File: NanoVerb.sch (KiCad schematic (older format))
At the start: 2 parts, among them U6 7805

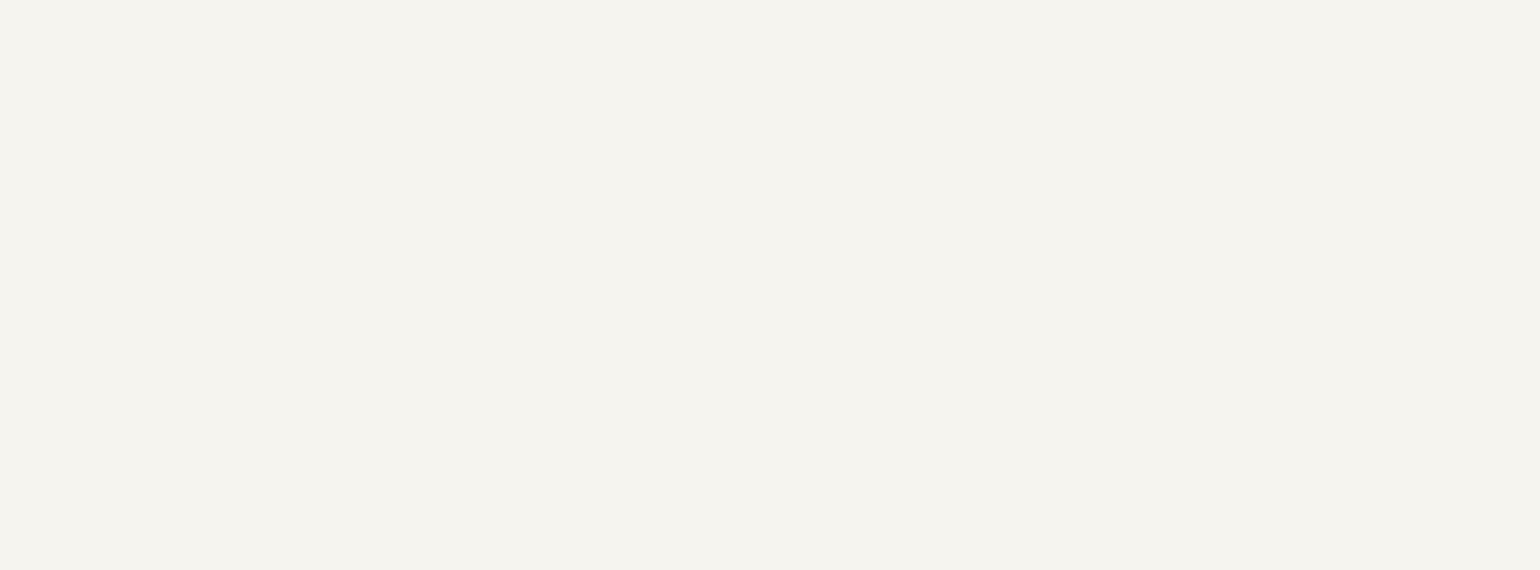
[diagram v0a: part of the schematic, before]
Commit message: Adding a few component symbols to the schematics (U9 and U8 OpAmps)
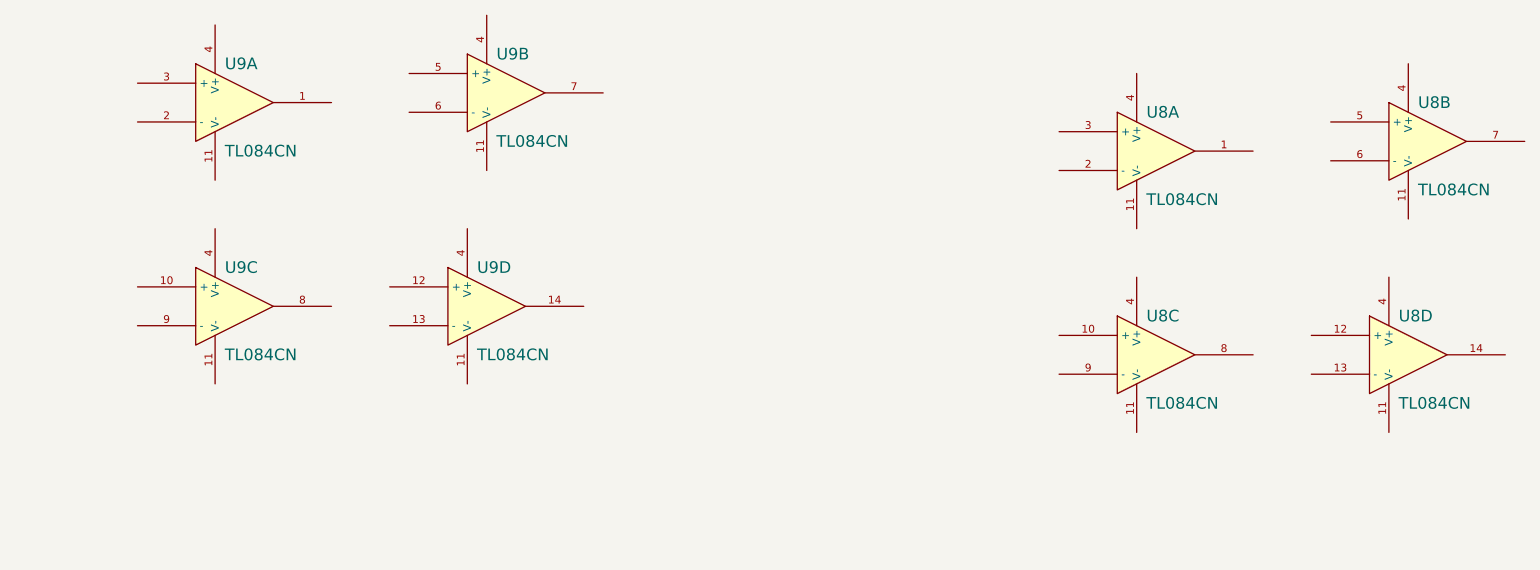
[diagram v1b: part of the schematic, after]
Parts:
- added U8, U9: TL084CN, symbol TL084CN
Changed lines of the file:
@@
 LIBS:valves
 LIBS:s87c51
+LIBS:tl084cn
 LIBS:NanoVerb-cache
 EELAYER 25 0
@@
 	1    0    0    -1
 $EndComp
+$Comp
+L TL084CN U9
+U 1 1 54A6F65E
+P 9150 2400
+F 0 "U9" H 9100 2600 60  0000 L CNN
+F 1 "TL084CN" H 9100 2150 60  0000 L CNN
+F 2 "" H 9150 2400 60  0000 C CNN
+F 3 "" H 9150 2400 60  0000 C CNN
+	1    9150 2400
+	1    0    0    -1
+$EndComp
+$Comp
+L TL084CN U9
+U 3 1 54A6F6C1
+P 9150 3450
+F 0 "U9" H 9100 3650 60  0000 L CNN
+F 1 "TL084CN" H 9100 3200 60  0000 L CNN
+F 2 "" H 9150 3450 60  0000 C CNN
+F 3 "" H 9150 3450 60  0000 C CNN
+	3    9150 3450
+	1    0    0    -1
+$EndComp
+$Comp
+L TL084CN U9
+U 4 1 54A6F6FF
+P 10450 3450
+F 0 "U9" H 10400 3650 60  0000 L CNN
+F 1 "TL084CN" H 10400 3200 60  0000 L CNN
+F 2 "" H 10450 3450 60  0000 C CNN
+F 3 "" H 10450 3450 60  0000 C CNN
+	4    10450 3450
+	1    0    0    -1
+$EndComp
+$Comp
+L TL084CN U9
+U 2 1 54A6F73C
+P 10550 2350
+F 0 "U9" H 10500 2550 60  0000 L CNN
+F 1 "TL084CN" H 10500 2100 60  0000 L CNN
+F 2 "" H 10550 2350 60  0000 C CNN
+F 3 "" H 10550 2350 60  0000 C CNN
+	2    10550 2350
+	1    0    0    -1
+$EndComp
+$Comp
+L TL084CN U8
+U 1 1 54A6FB5C
+P 13900 2650
+F 0 "U8" H 13850 2850 60  0000 L CNN
+F 1 "TL084CN" H 13850 2400 60  0000 L CNN
+F 2 "" H 13900 2650 60  0000 C CNN
+F 3 "" H 13900 2650 60  0000 C CNN
+	1    13900 2650
+	1    0    0    -1
+$EndComp
+$Comp
+L TL084CN U8
+U 3 1 54A6FB62
+P 13900 3700
+F 0 "U8" H 13850 3900 60  0000 L CNN
+F 1 "TL084CN" H 13850 3450 60  0000 L CNN
+F 2 "" H 13900 3700 60  0000 C CNN
+F 3 "" H 13900 3700 60  0000 C CNN
+	3    13900 3700
+	1    0    0    -1
+$EndComp
+$Comp
+L TL084CN U8
+U 4 1 54A6FB68
+P 15200 3700
+F 0 "U8" H 15150 3900 60  0000 L CNN
+F 1 "TL084CN" H 15150 3450 60  0000 L CNN
+F 2 "" H 15200 3700 60  0000 C CNN
+F 3 "" H 15200 3700 60  0000 C CNN
+	4    15200 3700
+	1    0    0    -1
+$EndComp
+$Comp
+L TL084CN U8
+U 2 1 54A6FB6E
+P 15300 2600
+F 0 "U8" H 15250 2800 60  0000 L CNN
+F 1 "TL084CN" H 15250 2350 60  0000 L CNN
+F 2 "" H 15300 2600 60  0000 C CNN
+F 3 "" H 15300 2600 60  0000 C CNN
+	2    15300 2600
+	1    0    0    -1
+$EndComp

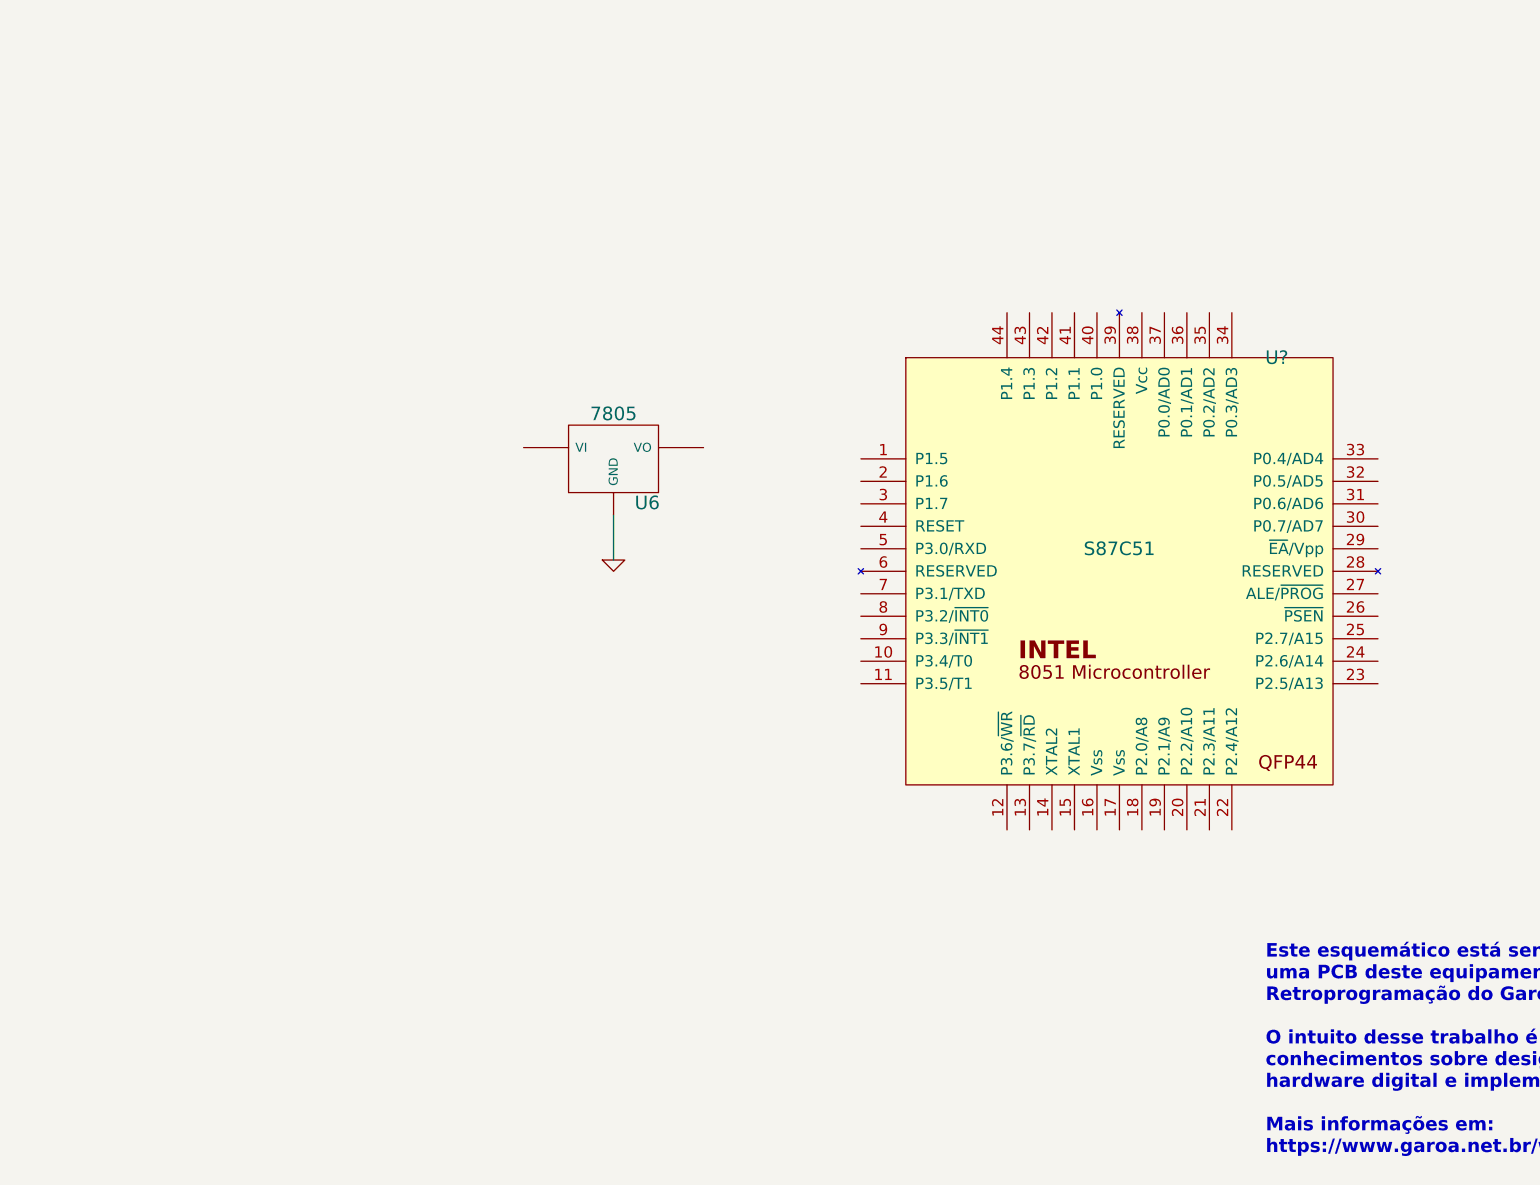
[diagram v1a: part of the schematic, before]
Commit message: updating schematics drawing with DRAM IC
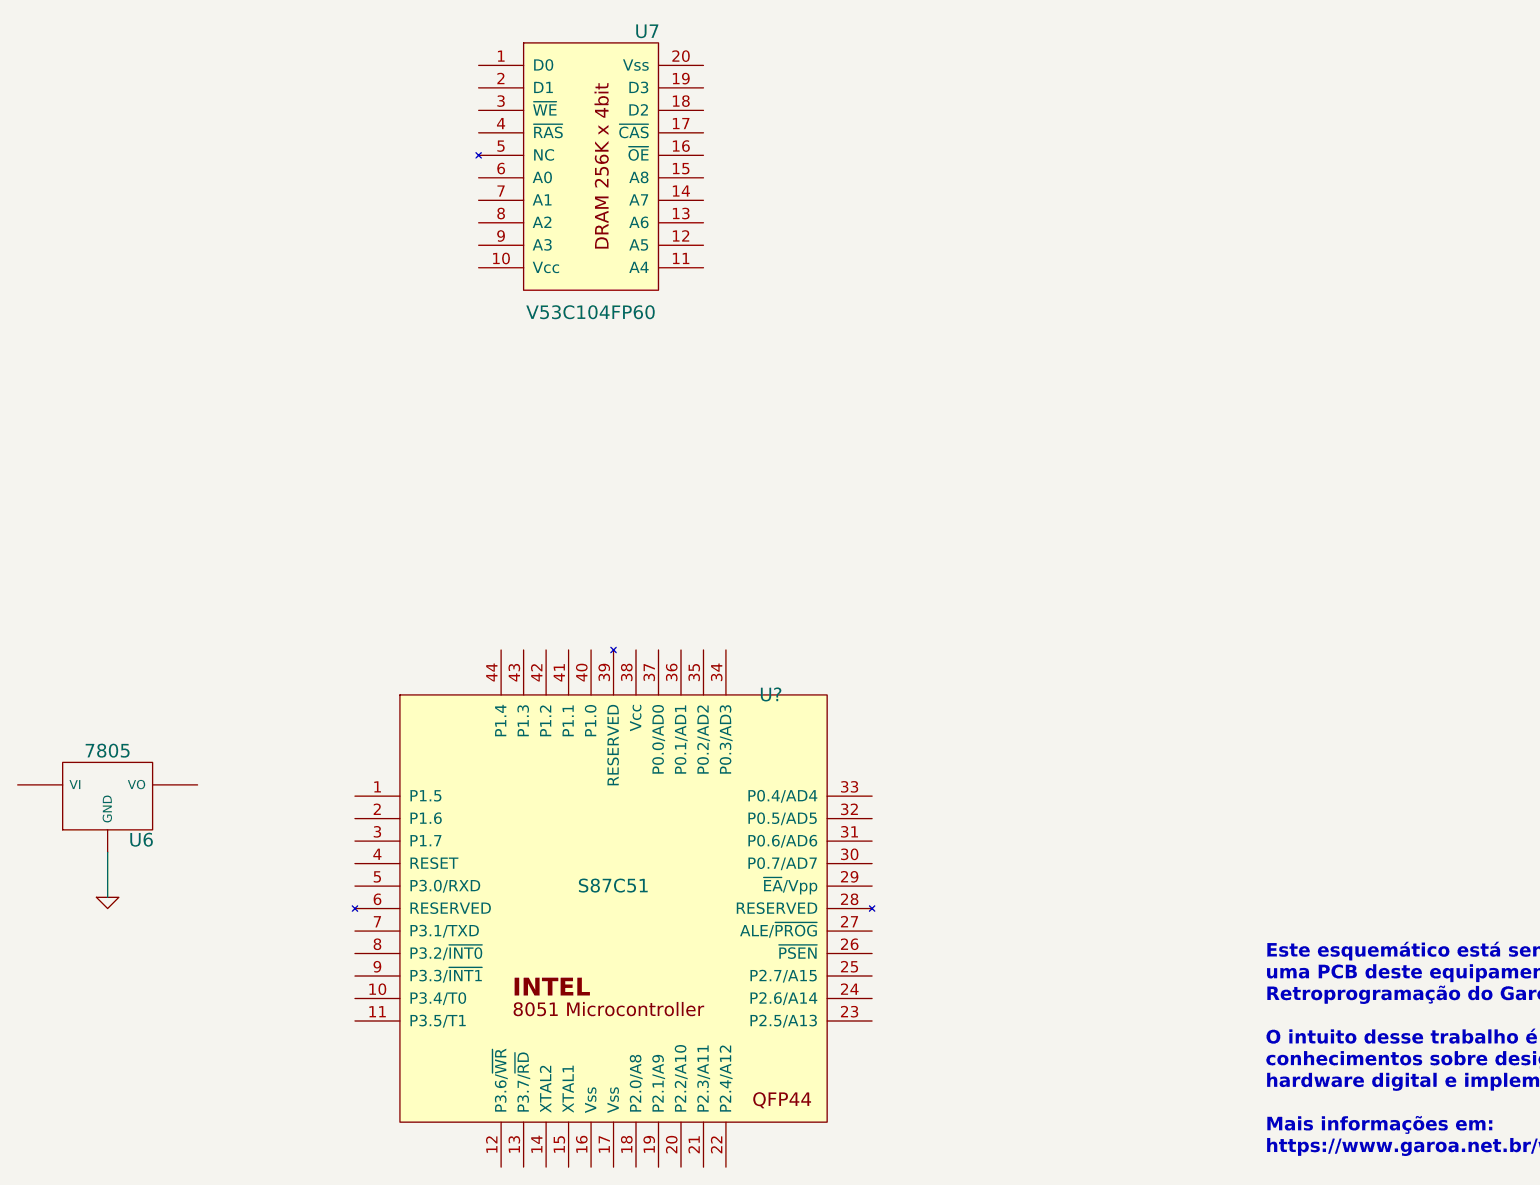
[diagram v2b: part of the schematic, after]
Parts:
- added U7: V53C104FP60, symbol V53C104FP60
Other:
- moved on the sheet: U6, U?
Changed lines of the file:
@@
 LIBS:s87c51
 LIBS:tl084cn
+LIBS:v53c104fp60
 LIBS:NanoVerb-cache
 EELAYER 25 0
@@
 L 7805 U6
 U 1 1 54A6E5DC
-P 4100 3350
-F 0 "U6" H 4250 3154 60  0000 C CNN
-F 1 "7805" H 4100 3550 60  0000 C CNN
-F 2 "" H 4100 3350 60  0000 C CNN
-F 3 "" H 4100 3350 60  0000 C CNN
-	1    4100 3350
+P 1850 4850
+F 0 "U6" H 2000 4654 60  0000 C CNN
+F 1 "7805" H 1850 5050 60  0000 C CNN
+F 2 "" H 1850 4850 60  0000 C CNN
+F 3 "" H 1850 4850 60  0000 C CNN
+	1    1850 4850
 	1    0    0    -1
 $EndComp
@@
 L GND #PWR?
 U 1 1 54A6E8E7
-P 4100 3800
-F 0 "#PWR?" H 4100 3800 30  0001 C CNN
-F 1 "GND" H 4100 3730 30  0001 C CNN
-F 2 "" H 4100 3800 60  0000 C CNN
-F 3 "" H 4100 3800 60  0000 C CNN
-	1    4100 3800
+P 1850 5300
+F 0 "#PWR?" H 1850 5300 30  0001 C CNN
+F 1 "GND" H 1850 5230 30  0001 C CNN
+F 2 "" H 1850 5300 60  0000 C CNN
+F 3 "" H 1850 5300 60  0000 C CNN
+	1    1850 5300
 	1    0    0    -1
 $EndComp
 Wire Wire Line
-	4100 3800 4100 3600
+	1850 5300 1850 5100
 $Comp
 L S87C51 U?
 U 1 1 54A6F801
-P 6350 3850
-F 0 "U?" H 7050 4800 60  0000 C CNN
-F 1 "S87C51" H 6350 3950 60  0000 C CNN
-F 2 "" H 6350 3850 60  0000 C CNN
-F 3 "" H 6350 3850 60  0000 C CNN
-	1    6350 3850
+P 4100 5350
+F 0 "U?" H 4800 6300 60  0000 C CNN
+F 1 "S87C51" H 4100 5450 60  0000 C CNN
+F 2 "" H 4100 5350 60  0000 C CNN
+F 3 "" H 4100 5350 60  0000 C CNN
+	1    4100 5350
 	1    0    0    -1
 $EndComp
@@
 	1    0    0    -1
 $EndComp
+$Comp
+L V53C104FP60 U7
+U 1 1 54A70A30
+P 4000 2050
+F 0 "U7" H 4250 2650 60  0000 C CNN
+F 1 "V53C104FP60" H 4000 1400 60  0000 C CNN
+F 2 "" H 4000 2200 60  0000 C CNN
+F 3 "" H 4000 2200 60  0000 C CNN
+	1    4000 2050
+	1    0    0    -1
+$EndComp
